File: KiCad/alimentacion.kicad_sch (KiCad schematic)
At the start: 6 parts, among them J1 Conn_01x02_Pin, U4 LT1117-3.3, U5 TSR3-2450N

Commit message: calefactor-Usart
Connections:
- net 5V: now reaches C4.1, U4.3 (VI), U5.3 (Vout)
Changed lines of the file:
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@@
+		)
+	)
+	(global_label "5V"
+		(shape input)
+		(at 119.38 71.12 90)
+		(fields_autoplaced yes)
+		(effects
+			(font
+				(size 1.27 1.27)
+			)
+			(justify left)
+		)
+		(property "Intersheetrefs" "${INTERSHEET_REFS}"
+			(at 119.38 65.8367 90)
+			(effects
+				(font
+					(size 1.27 1.27)
+				)
+				(justify left)
+				(hide yes)
+			)
 		)
 	)

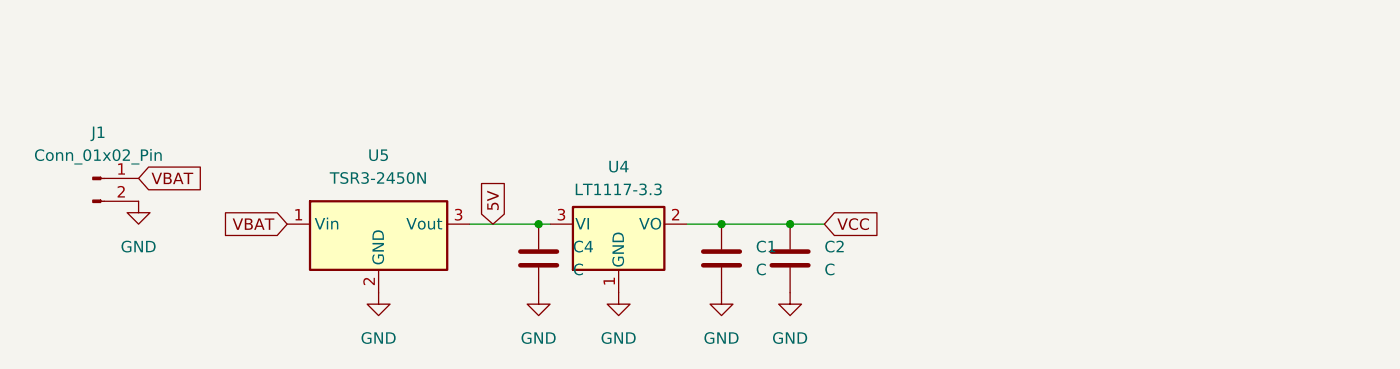
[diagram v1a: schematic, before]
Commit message: canvis organització y reles calefactor
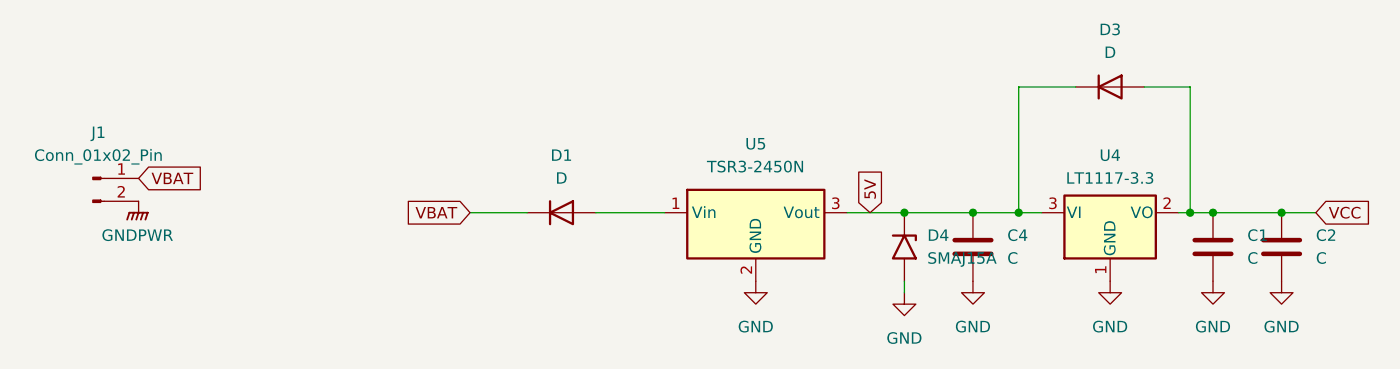
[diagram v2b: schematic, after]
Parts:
- added D1, D3: D, symbol Device:D
- added D4: SMAJ15A, Diode_SMD:D_SMA, symbol Diode:SMAJ15A
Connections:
- net 5V: now also D3.1 (K), D4.1 (A1)
- net GND: now also D4.2 (A2); no longer J1.2 (Pin_2)
- net VBAT: now also D1.1 (K); no longer U5.1 (Vin)
- net VCC: now also D3.2 (A)
- new net: D1.2 (A), U5.1 (Vin)
- new net GNDPWR: J1.2 (Pin_2)
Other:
- moved on the sheet: C1, C2, C4, U4, U5

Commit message: he añadido huelas a algunos componentes importates
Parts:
- J1: footprint (none) -> Connector_PinHeader_2.54mm:PinHeader_1x02_P2.54mm_Vertical
- U4: footprint (none) -> Package_TO_SOT_SMD:SOT-223-3_TabPin2
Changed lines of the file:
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@@
+	)
+	(junction
+		(at 161.29 69.85)
+		(diameter 0)
+		(color 0 0 0 0)
 	)
 	(junction
@@
 	(wire
 		(pts
+			(xy 161.29 69.85) (xy 165.1 69.85)
+		)
+		(stroke
+			(width 0)
+			(type default)
+		)
+	)
+	(wire
+		(pts
 			(xy 172.72 69.85) (xy 177.8 69.85)
 		)
@@
 	(wire
 		(pts
-			(xy 207.01 69.85) (xy 210.82 69.85)
-		)
-		(stroke
-			(width 0)
-			(type default)
-		)
-	)
-	(wire
-		(pts
 			(xy 123.19 69.85) (xy 116.84 69.85)
 		)
@@
 	(wire
 		(pts
-			(xy 158.75 69.85) (xy 165.1 69.85)
+			(xy 158.75 69.85) (xy 161.29 69.85)
 		)
 		(stroke
@@
 	(wire
 		(pts
+			(xy 213.36 69.85) (xy 207.01 69.85)
+		)
+		(stroke
+			(width 0)
+			(type default)
+		)
+	)
+	(wire
+		(pts
 			(xy 195.58 69.85) (xy 196.85 69.85)
 		)
@@
 		(pts
 			(xy 165.1 69.85) (xy 172.72 69.85)
+		)
+		(stroke
+			(width 0)
+			(type default)
+		)
+	)
+	(wire
+		(pts
+			(xy 161.29 60.96) (xy 161.29 69.85)
+		)
+		(stroke
+			(width 0)
+			(type default)
+		)
+	)
+	(wire
+		(pts
+			(xy 213.36 62.23) (xy 213.36 69.85)
 		)
 		(stroke
@@
 	(global_label "VCC"
 		(shape input)
-		(at 210.82 69.85 0)
+		(at 213.36 62.23 90)
 		(fields_autoplaced yes)
 		(effects
@@
 		)
 		(property "Intersheetrefs" "${INTERSHEET_REFS}"
-			(at 217.4338 69.85 0)
+			(at 213.36 55.6162 90)
 			(effects
 				(font
@@
 	(global_label "5V"
 		(shape input)
-		(at 161.29 69.85 90)
+		(at 161.29 60.96 90)
 		(fields_autoplaced yes)
 		(effects
@@
 		)
 		(property "Intersheetrefs" "${INTERSHEET_REFS}"
-			(at 161.29 64.5667 90)
+			(at 161.29 55.6767 90)
 			(effects
 				(font
@@
 			)
 		)
-		(property "Footprint" ""
+		(property "Footprint" "Connector_PinHeader_2.54mm:PinHeader_1x02_P2.54mm_Vertical"
 			(at 74.93 66.04 0)
 			(effects
@@
 			)
 		)
-		(property "Footprint" ""
+		(property "Footprint" "Package_TO_SOT_SMD:SOT-223-3_TabPin2"
 			(at 187.96 69.85 0)
 			(effects

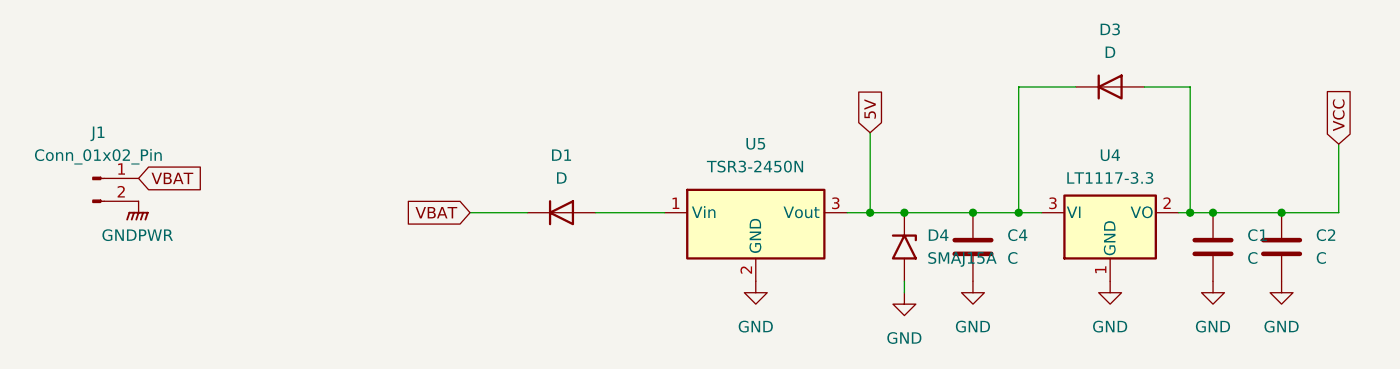
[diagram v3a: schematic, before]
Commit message: he añadido el resto de huellas, he corregido algunos errores en la parte de alimentación en los diodos. tambien he trasladados todas las huellas a la pcb y lo he intentado separar un poco para verlo mas claro cuando empecemos el placing.
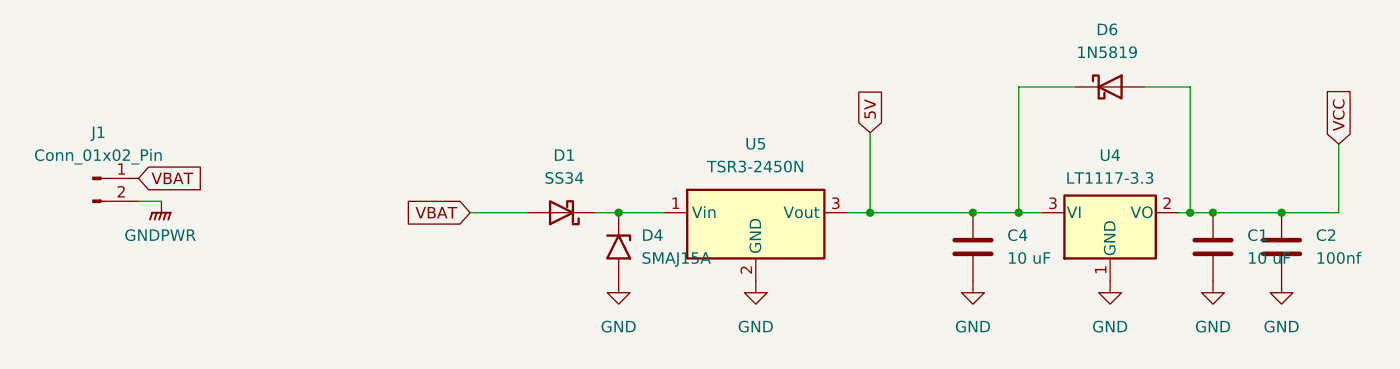
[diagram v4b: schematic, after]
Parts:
- removed D1, D3: D, symbol Device:D
- added D1: SS34, Diode_SMD:D_SMA, symbol Diode:SS34
- added D6: 1N5819, Diode_THT:D_DO-41_SOD81_P10.16mm_Horizontal, symbol Diode:1N5819
- C1, C4: value C -> 10 uF; footprint (none) -> Capacitor_THT:CP_Radial_D4.0mm_P1.50mm
- C2: value C -> 100nf; footprint (none) -> Capacitor_SMD:C_0402_1005Metric
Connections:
- net 5V: now also D6.1 (K); no longer D4.1 (A1)
- net VBAT: now also D1.2 (A)
- net VCC: now also D6.2 (A)
- net at U5.1 (Vin): now also D4.1 (A1), D1.1 (K)
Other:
- moved on the sheet: D4

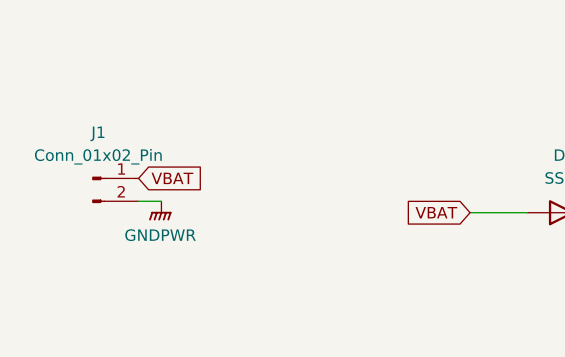
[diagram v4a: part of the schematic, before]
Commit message: añadido test points y solucionado un error con gnd en alimentación
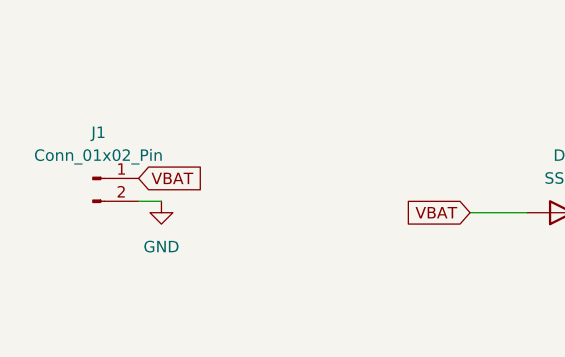
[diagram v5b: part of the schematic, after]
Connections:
- net GNDPWR is gone; now on net GND: J1.2 (Pin_2)
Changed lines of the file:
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@@
 		)
 		(instances
+			(project "alimentacion"
+				(path "/488d7143-5cfe-4655-8097-bbd968af1df0"
+					(reference "J?")
+					(unit 1)
+				)
+			)
 			(project "Retrovisores"
 				(path "/9b9f005f-0621-4675-bd4e-683e7082b120/69d3243c-3079-440e-aee4-a9c749ca40e1"
@@
 		)
 		(instances
+			(project "alimentacion"
+				(path "/488d7143-5cfe-4655-8097-bbd968af1df0"
+					(reference "U?")
+					(unit 1)
+				)
+			)
 			(project "Retrovisores"
 				(path "/9b9f005f-0621-4675-bd4e-683e7082b120/69d3243c-3079-440e-aee4-a9c749ca40e1"
@@
 		)
 		(instances
+			(project "alimentacion"
+				(path "/488d7143-5cfe-4655-8097-bbd968af1df0"
+					(reference "#PWR?")
+					(unit 1)
+				)
+			)
 			(project "Retrovisores"
 				(path "/9b9f005f-0621-4675-bd4e-683e7082b120/69d3243c-3079-440e-aee4-a9c749ca40e1"
@@
 		)
 		(instances
+			(project "alimentacion"
+				(path "/488d7143-5cfe-4655-8097-bbd968af1df0"
+					(reference "#PWR?")
+					(unit 1)
+				)
+			)
 			(project "Retrovisores"
 				(path "/9b9f005f-0621-4675-bd4e-683e7082b120/69d3243c-3079-440e-aee4-a9c749ca40e1"
@@
 		)
 		(instances
+			(project "alimentacion"
+				(path "/488d7143-5cfe-4655-8097-bbd968af1df0"
+					(reference "U?")
+					(unit 1)
+				)
+			)
 			(project "Retrovisores"
 				(path "/9b9f005f-0621-4675-bd4e-683e7082b120/69d3243c-3079-440e-aee4-a9c749ca40e1"
@@
 		)
 		(instances
+			(project "alimentacion"
+				(path "/488d7143-5cfe-4655-8097-bbd968af1df0"
+					(reference "#PWR?")
+					(unit 1)
+				)
+			)
 			(project "Retrovisores"
 				(path "/9b9f005f-0621-4675-bd4e-683e7082b120/69d3243c-3079-440e-aee4-a9c749ca40e1"
@@
 		)
 		(instances
+			(project "alimentacion"
+				(path "/488d7143-5cfe-4655-8097-bbd968af1df0"
+					(reference "C?")
+					(unit 1)
+				)
+			)
 			(project "Retrovisores"
 				(path "/9b9f005f-0621-4675-bd4e-683e7082b120/69d3243c-3079-440e-aee4-a9c749ca40e1"
@@
 		)
 		(instances
+			(project "alimentacion"
+				(path "/488d7143-5cfe-4655-8097-bbd968af1df0"
+					(reference "D?")
+					(unit 1)
+				)
+			)
 			(project "Retrovisores"
 				(path "/9b9f005f-0621-4675-bd4e-683e7082b120/69d3243c-3079-440e-aee4-a9c749ca40e1"
@@
 		)
 		(instances
+			(project "alimentacion"
+				(path "/488d7143-5cfe-4655-8097-bbd968af1df0"
+					(reference "C?")
+					(unit 1)
+				)
+			)
 			(project "Retrovisores"
 				(path "/9b9f005f-0621-4675-bd4e-683e7082b120/69d3243c-3079-440e-aee4-a9c749ca40e1"
@@
 		)
 		(instances
+			(project "alimentacion"
+				(path "/488d7143-5cfe-4655-8097-bbd968af1df0"
+					(reference "#PWR?")
+					(unit 1)
+				)
+			)
 			(project "Retrovisores"
 				(path "/9b9f005f-0621-4675-bd4e-683e7082b120/69d3243c-3079-440e-aee4-a9c749ca40e1"
@@
 		)
 		(instances
+			(project "alimentacion"
+				(path "/488d7143-5cfe-4655-8097-bbd968af1df0"
+					(reference "D?")
+					(unit 1)
+				)
+			)
 			(project ""
 				(path "/9b9f005f-0621-4675-bd4e-683e7082b120/69d3243c-3079-440e-aee4-a9c749ca40e1"
 					(reference "D1")
-					(unit 1)
-				)
-			)
-		)
-	)
-	(symbol
-		(lib_id "power:GNDPWR")
-		(at 82.55 68.58 0)
-		(unit 1)
-		(exclude_from_sim no)
-		(in_bom yes)
-		(on_board yes)
-		(dnp no)
-		(fields_autoplaced yes)
-		(property "Reference" "#PWR017"
-			(at 82.55 73.66 0)
-			(effects
-				(font
-					(size 1.27 1.27)
-				)
-				(hide yes)
-			)
-		)
-		(property "Value" "GNDPWR"
-			(at 82.423 72.39 0)
-			(effects
-				(font
-					(size 1.27 1.27)
-				)
-			)
-		)
-		(property "Footprint" ""
-			(at 82.55 69.85 0)
-			(effects
-				(font
-					(size 1.27 1.27)
-				)
-				(hide yes)
-			)
-		)
-		(property "Datasheet" ""
-			(at 82.55 69.85 0)
-			(effects
-				(font
-					(size 1.27 1.27)
-				)
-				(hide yes)
-			)
-		)
-		(property "Description" "Power symbol creates a global label with name \"GNDPWR\" , global ground"
-			(at 82.55 68.58 0)
-			(effects
-				(font
-					(size 1.27 1.27)
-				)
-				(hide yes)
-			)
-		)
-		(pin "1"
-		)
-		(instances
-			(project ""
-				(path "/9b9f005f-0621-4675-bd4e-683e7082b120/69d3243c-3079-440e-aee4-a9c749ca40e1"
-					(reference "#PWR017")
 					(unit 1)
 				)
@@
 		)
 		(instances
+			(project "alimentacion"
+				(path "/488d7143-5cfe-4655-8097-bbd968af1df0"
+					(reference "C?")
+					(unit 1)
+				)
+			)
 			(project "Retrovisores"
 				(path "/9b9f005f-0621-4675-bd4e-683e7082b120/69d3243c-3079-440e-aee4-a9c749ca40e1"
@@
 		)
 		(instances
+			(project "alimentacion"
+				(path "/488d7143-5cfe-4655-8097-bbd968af1df0"
+					(reference "#PWR?")
+					(unit 1)
+				)
+			)
 			(project "Retrovisores"
 				(path "/9b9f005f-0621-4675-bd4e-683e7082b120/69d3243c-3079-440e-aee4-a9c749ca40e1"
@@
 		)
 		(instances
+			(project "alimentacion"
+				(path "/488d7143-5cfe-4655-8097-bbd968af1df0"
+					(reference "D?")
+					(unit 1)
+				)
+			)
 			(project ""
 				(path "/9b9f005f-0621-4675-bd4e-683e7082b120/69d3243c-3079-440e-aee4-a9c749ca40e1"
@@
 		)
 		(instances
+			(project "alimentacion"
+				(path "/488d7143-5cfe-4655-8097-bbd968af1df0"
+					(reference "#PWR?")
+					(unit 1)
+				)
+			)
 			(project "Retrovisores"
 				(path "/9b9f005f-0621-4675-bd4e-683e7082b120/69d3243c-3079-440e-aee4-a9c749ca40e1"
@@
 		)
 	)
+	(symbol
+		(lib_id "power:GND")
+		(at 82.55 68.58 0)
+		(unit 1)
+		(exclude_from_sim no)
+		(in_bom yes)
+		(on_board yes)
+		(dnp no)
+		(fields_autoplaced yes)
+		(property "Reference" "#PWR?"
+			(at 82.55 74.93 0)
+			(effects
+				(font
+					(size 1.27 1.27)
+				)
+				(hide yes)
+			)
+		)
+		(property "Value" "GND"
+			(at 82.55 73.66 0)
+			(effects
+				(font
+					(size 1.27 1.27)
+				)
+			)
+		)
+		(property "Footprint" ""
+			(at 82.55 68.58 0)
+			(effects
+				(font
+					(size 1.27 1.27)
+				)
+				(hide yes)
+			)
+		)
+		(property "Datasheet" ""
+			(at 82.55 68.58 0)
+			(effects
+				(font
+					(size 1.27 1.27)
+				)
+				(hide yes)
+			)
+		)
+		(property "Description" "Power symbol creates a global label with name \"GND\" , ground"
+			(at 82.55 68.58 0)
+			(effects
+				(font
+					(size 1.27 1.27)
+				)
+				(hide yes)
+			)
+		)
+		(pin "1"
+		)
+		(instances
+			(project "alimentacion"
+				(path "/488d7143-5cfe-4655-8097-bbd968af1df0"
+					(reference "#PWR01")
+					(unit 1)
+				)
+			)
+			(project "Retrovisores"
+				(path "/9b9f005f-0621-4675-bd4e-683e7082b120/69d3243c-3079-440e-aee4-a9c749ca40e1"
+					(reference "#PWR?")
+					(unit 1)
+				)
+			)
+		)
+	)
+	(sheet_instances
+		(path "/"
+			(page "1")
+		)
+	)
+	(embedded_fonts no)
 )
